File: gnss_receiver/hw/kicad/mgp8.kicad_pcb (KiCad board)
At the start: 8 copper layers, 100 x 75 mm, 429 parts, among them X1 FTSH-105-01-L-DV-K, X2 FTSH-105-01-L-DV-K, X3 FTSH-105-01-L-DV-K, X4 M22-2510205, X5 SM06B-GHS-TB, X6 SM04B-GHS-TB, X7 SM04B-GHS-TB, X8 SM04B-SRSS-TB

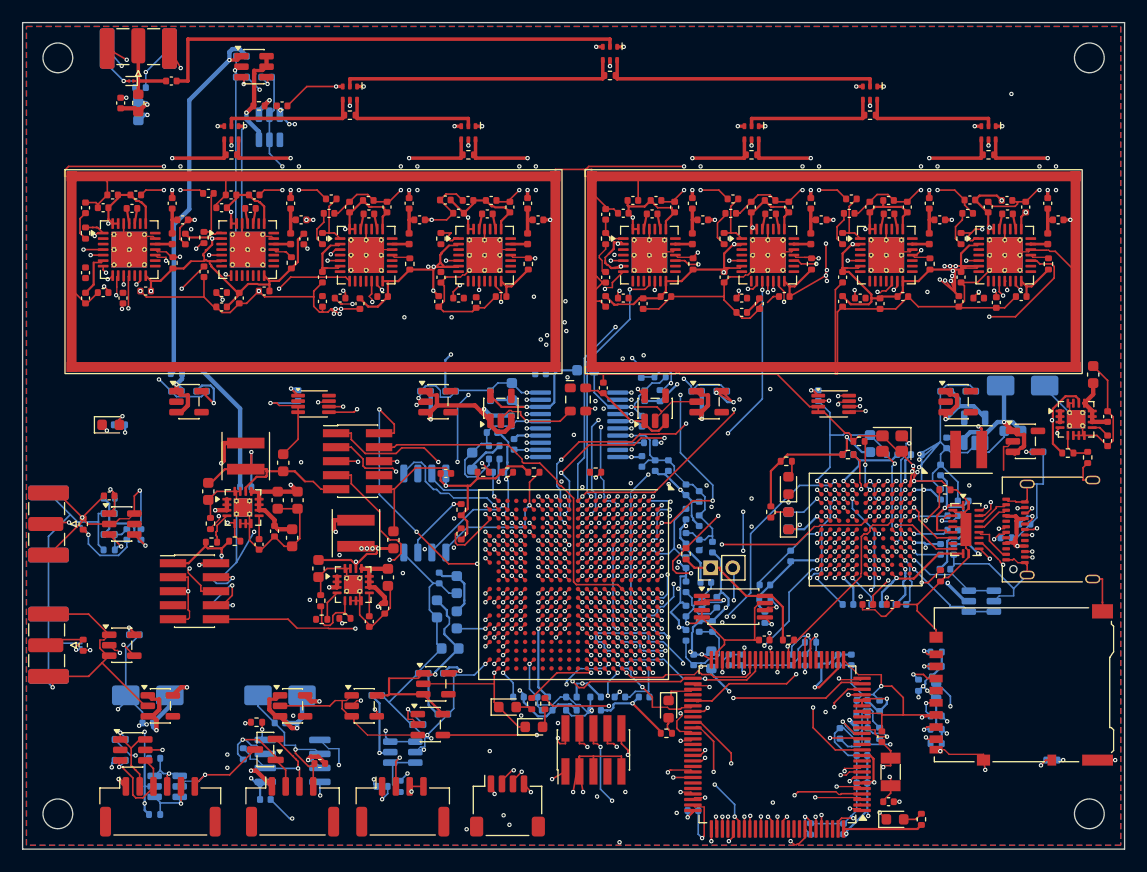
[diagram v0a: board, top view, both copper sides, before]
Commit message: МГП-8: доразводка платы волновым трассировщиком — 20 неразведённых соединений вместо 144
- hw/gen/pcb_maze.py — доразводка после Freerouting: волновой поиск на сетке 0,05 мм
  (длинные окна — 0,1 мм) по слоям L1, L3, L6, L8 и L4 в цифровой зоне (не под островками
  ВЧ- и тактового питания L5, не ближе 0,5 мм к линиям L3); перекладка мешающих проводников
  чужих цепей с откатом, если хоть одна цепь осталась разорванной; снятие висящих обрезков
  по отчёту DRC с проверкой, что KiCad по-прежнему видит соединения.
- Плата: не разведено 20 из 1140 (было 144), DRC без ошибок, схема и плата совпадают;
  проводников 8220, переходов 1233, длина 10,5 м. Остались 16 линий к верхним рядам шариков
  ПЛИС DD7 (каналы выхода из-под BGA заняты), SSTX_N, XTAL_A, REF_CMP_R, ANT_IMON_R.
- Пересчитаны масса (56,1 г) и тепловая модель по новому заполнению медью: Tj ПЛИС, МК и
  FX3 с отводом на крышку — не выше 92,8 °С, как и прежде.
- ПЗ 4.7.1, 4.7.2, 4.7.4, 4.7.5, 5.7.2, таблица 5, 9.1 п. 1; КД пересобрана.

Co-Authored-By: Claude Opus 5.5 <noreply@anthropic.com>
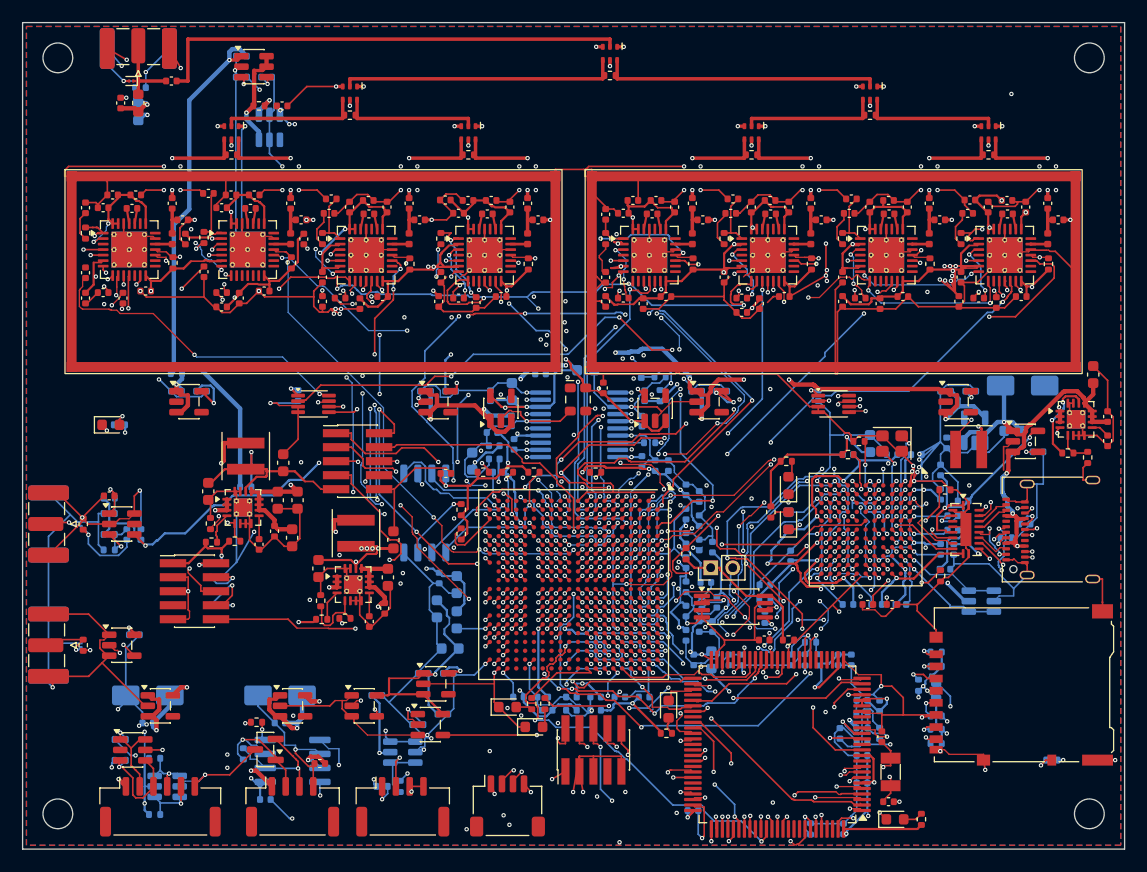
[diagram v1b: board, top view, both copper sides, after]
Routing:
- net MAX_SCLK: track 26.3 -> 130.5 mm, vias 4 -> 13
- net FX3_CSN_B: track 1.13 -> 85.1 mm, vias 2 -> 10
- net MAX_I0_H: track 0.57 -> 56.4 mm, vias 1 -> 5
- net FPGA_INITN: track 5.15 -> 58.2 mm, vias 2 -> 4
- net FX3_G3: track 1.13 -> 52.5 mm, vias 2 -> 8
- net MAX_SHDN_B: track 2.45 -> 53.7 mm, vias 1 -> 5
- net MAX_LD_B: track 0.57 -> 48.2 mm, vias 1 -> 5
- net MAX_Q0_C: track 0.57 -> 47.4 mm, vias 1 -> 6
- net MAX_CSN_C: track 0.57 -> 47.3 mm, vias 1 -> 4
- net MAX_SHDN_C: track 2.34 -> 49.0 mm, vias 1 -> 6
- net MAX_LD_D: track 0.57 -> 46.2 mm, vias 1 -> 5
- net MAX_LD_C: track 0.57 -> 46.1 mm, vias 1 -> 6
- net MAX_SDATA: track 78.0 -> 123.1 mm, vias 3 -> 13
- net +5V_SYS: track 193.4 -> 238.4 mm, vias 13 -> 20
- net MAX_Q0_D: track 0.57 -> 45.3 mm, vias 1 -> 8
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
